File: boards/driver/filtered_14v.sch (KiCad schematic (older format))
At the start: 2 parts

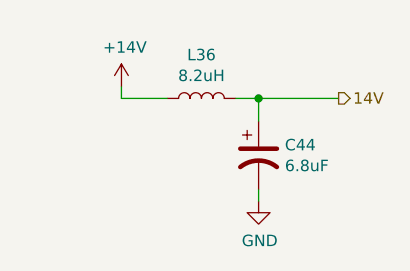
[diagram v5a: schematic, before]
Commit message: Driver board: largely fleshed out part selection
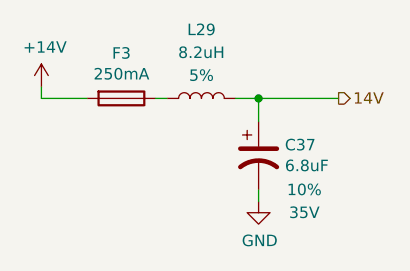
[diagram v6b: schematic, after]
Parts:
- added F2: 250mA, symbol Device:Fuse
- C3: Digikey (none) -> https://www.digikey.com/en/products/detail/kemet/T495D685K0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; ESR (none) -> 0.3; Part Number (none) -> T495D685K035ATE300; Rating (none) -> 35V; Tolerance (none) -> 10%
- L29: DCR (none) -> 1.40; Digikey (none) -> https://www.digikey.com/en/products/detail/api-delevan-inc/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; Part Number (none) -> 1812R-822J; Rating (none) -> 375mA; Tolerance (none) -> 5%
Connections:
- net +14V: now also F2.2; no longer L29.1
- new net: F2.1, L29.1
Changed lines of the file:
@@
 $Descr A4 11693 8268
 encoding utf-8
-Sheet 3 64
+Sheet 49 64
 Title ""
 Date ""
@@
 AR Path="/6183FAE6/61E0F0ED/625192D8" Ref="L?"  Part="1"
 AR Path="/61EC7443/61E13129/625192D8" Ref="L1"  Part="1"
-F 0 "L36" V 5490 3800 50  0000 C CNN
-F 1 "8.2uH" V 5399 3800 50  0000 C CNN
+F 0 "L29" V 5600 3800 50  0000 C CNN
+F 1 "8.2uH" V 5500 3800 50  0000 C CNN
 F 2 "Inductor_SMD:L_1812_4532Metric" H 5300 3800 50  0001 C CNN
 F 3 "~" H 5300 3800 50  0001 C CNN
+F 4 "5%" V 5400 3800 50  0000 C CNN "Tolerance"
+F 5 "1.40" V 5300 3800 50  0001 C CNN "DCR"
+F 6 "375mA" V 5300 3800 50  0001 C CNN "Rating"
+F 7 "1812R-822J" V 5300 3800 50  0001 C CNN "Part Number"
+F 8 "https://www.digikey.com/en/products/detail/api-delevan-inc/1812R-822J/1115322" V 5300 3800 50  0001 C CNN "Digikey"
 	1    5300 3800
 	0    -1   -1   0
@@
 L lachesis:+14V #PWR0105
 U 1 1 62519A3E
-P 4950 3750
+P 4600 3750
 AR Path="/6183FAE6/62519032/62519A3E" Ref="#PWR0105"  Part="1"
 AR Path="/6183FAE6/62531DCA/62519A3E" Ref="#PWR0107"  Part="1"
@@
 AR Path="/6183FAE6/61E0F0ED/62519A3E" Ref="#PWR?"  Part="1"
 AR Path="/61EC7443/61E13129/62519A3E" Ref="#PWR05"  Part="1"
-F 0 "#PWR0119" H 4950 3600 50  0001 C CNN
-F 1 "+14V" H 4965 3923 50  0000 C CNN
-F 2 "" H 4950 3750 50  0001 C CNN
-F 3 "" H 4950 3750 50  0001 C CNN
-	1    4950 3750
+F 0 "#PWR0119" H 4600 3600 50  0001 C CNN
+F 1 "+14V" H 4615 3923 50  0000 C CNN
+F 2 "" H 4600 3750 50  0001 C CNN
+F 3 "" H 4600 3750 50  0001 C CNN
+	1    4600 3750
 	1    0    0    -1
 $EndComp
 Wire Wire Line
-	4950 3750 4950 3800
-Wire Wire Line
-	4950 3800 5150 3800
+	4600 3750 4600 3800
 Wire Wire Line
 	5450 3800 5550 3800
@@
 AR Path="/6183FAE6/626621BA/628400BF" Ref="C43"  Part="1"
 AR Path="/6183FAE6/626621BF/628400BF" Ref="C44"  Part="1"
-F 0 "C44" H 5665 4096 50  0000 L CNN
+F 0 "C37" H 5665 4096 50  0000 L CNN
 F 1 "6.8uF" H 5665 4005 50  0000 L CNN
 F 2 "Capacitor_Tantalum_SMD:CP_EIA-7343-31_Kemet-D" H 5550 4050 50  0001 C CNN
 F 3 "~" H 5550 4050 50  0001 C CNN
+F 4 "10%" H 5750 3900 50  0000 C CNN "Tolerance"
+F 5 "35V" H 5750 3800 50  0000 C CNN "Rating"
+F 6 "0.3" H 5550 4050 50  0001 C CNN "ESR"
+F 7 "T495D685K035ATE300" H 5550 4050 50  0001 C CNN "Part Number"
+F 8 "https://www.digikey.com/en/products/detail/kemet/T495D685K035ATE300/4309257" H 5550 4050 50  0001 C CNN "Digikey"
 	1    5550 4050
 	1    0    0    -1
 $EndComp
+$Comp
+L Device:Fuse F2
+U 1 1 61D37A88
+P 4950 3800
+AR Path="/64D2DF1E/62A035A1/61D37A88" Ref="F2"  Part="1"
+AR Path="/6183FAE6/62531DCA/61D37A88" Ref="F4"  Part="1"
+AR Path="/61EC7443/61E13129/61D37A88" Ref="F1"  Part="1"
+AR Path="/6183FAE6/62519032/61D37A88" Ref="F3"  Part="1"
+AR Path="/6183FAE6/6254620B/61D37A88" Ref="F5"  Part="1"
+AR Path="/6183FAE6/62630A14/61D37A88" Ref="F6"  Part="1"
+AR Path="/6183FAE6/62637D4C/61D37A88" Ref="F7"  Part="1"
+AR Path="/6183FAE6/626621B6/61D37A88" Ref="F8"  Part="1"
+AR Path="/6183FAE6/626621BA/61D37A88" Ref="F9"  Part="1"
+AR Path="/6183FAE6/626621BF/61D37A88" Ref="F10"  Part="1"
+F 0 "F3" V 4753 3800 50  0000 C CNN
+F 1 "250mA" V 4844 3800 50  0000 C CNN
+F 2 "" V 4880 3800 50  0001 C CNN
+F 3 "~" H 4950 3800 50  0001 C CNN
+	1    4950 3800
+	0    1    1    0
+$EndComp
+Wire Wire Line
+	5150 3800 5100 3800
+Wire Wire Line
+	4800 3800 4600 3800
 $EndSCHEMATC
